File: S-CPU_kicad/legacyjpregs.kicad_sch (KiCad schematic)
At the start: 52 parts

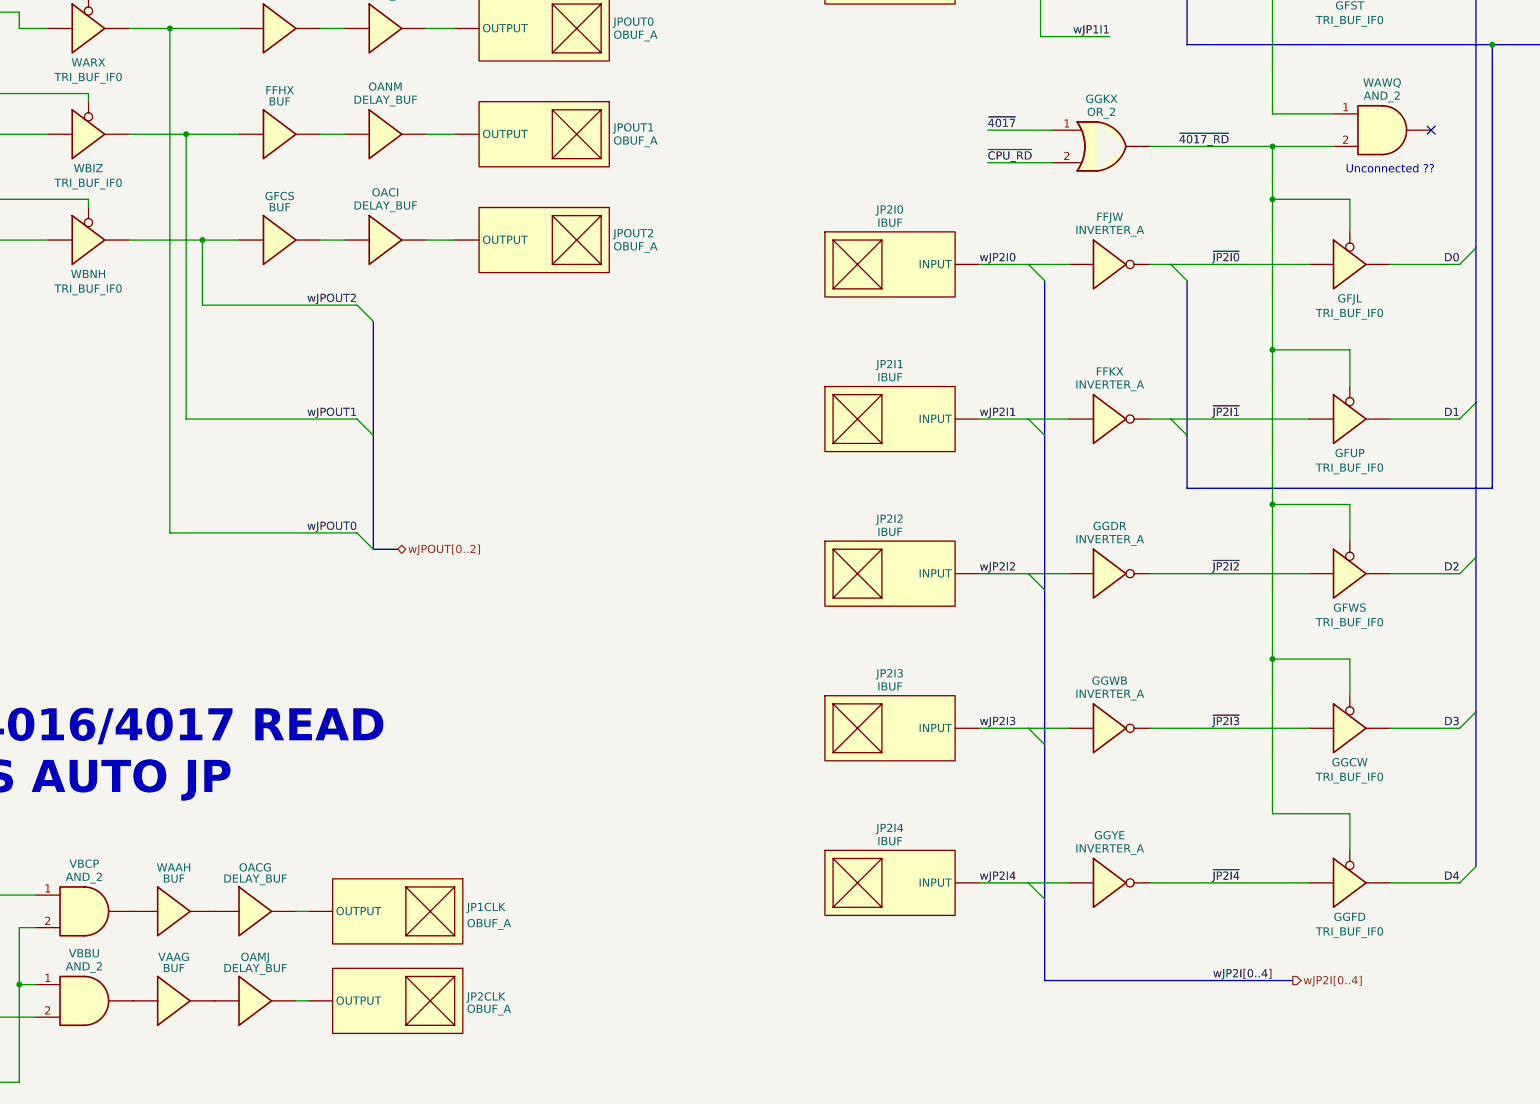
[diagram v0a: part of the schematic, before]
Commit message: Fixed VAWR which should have been an SR DFF (to fix issue #3 raised in github)
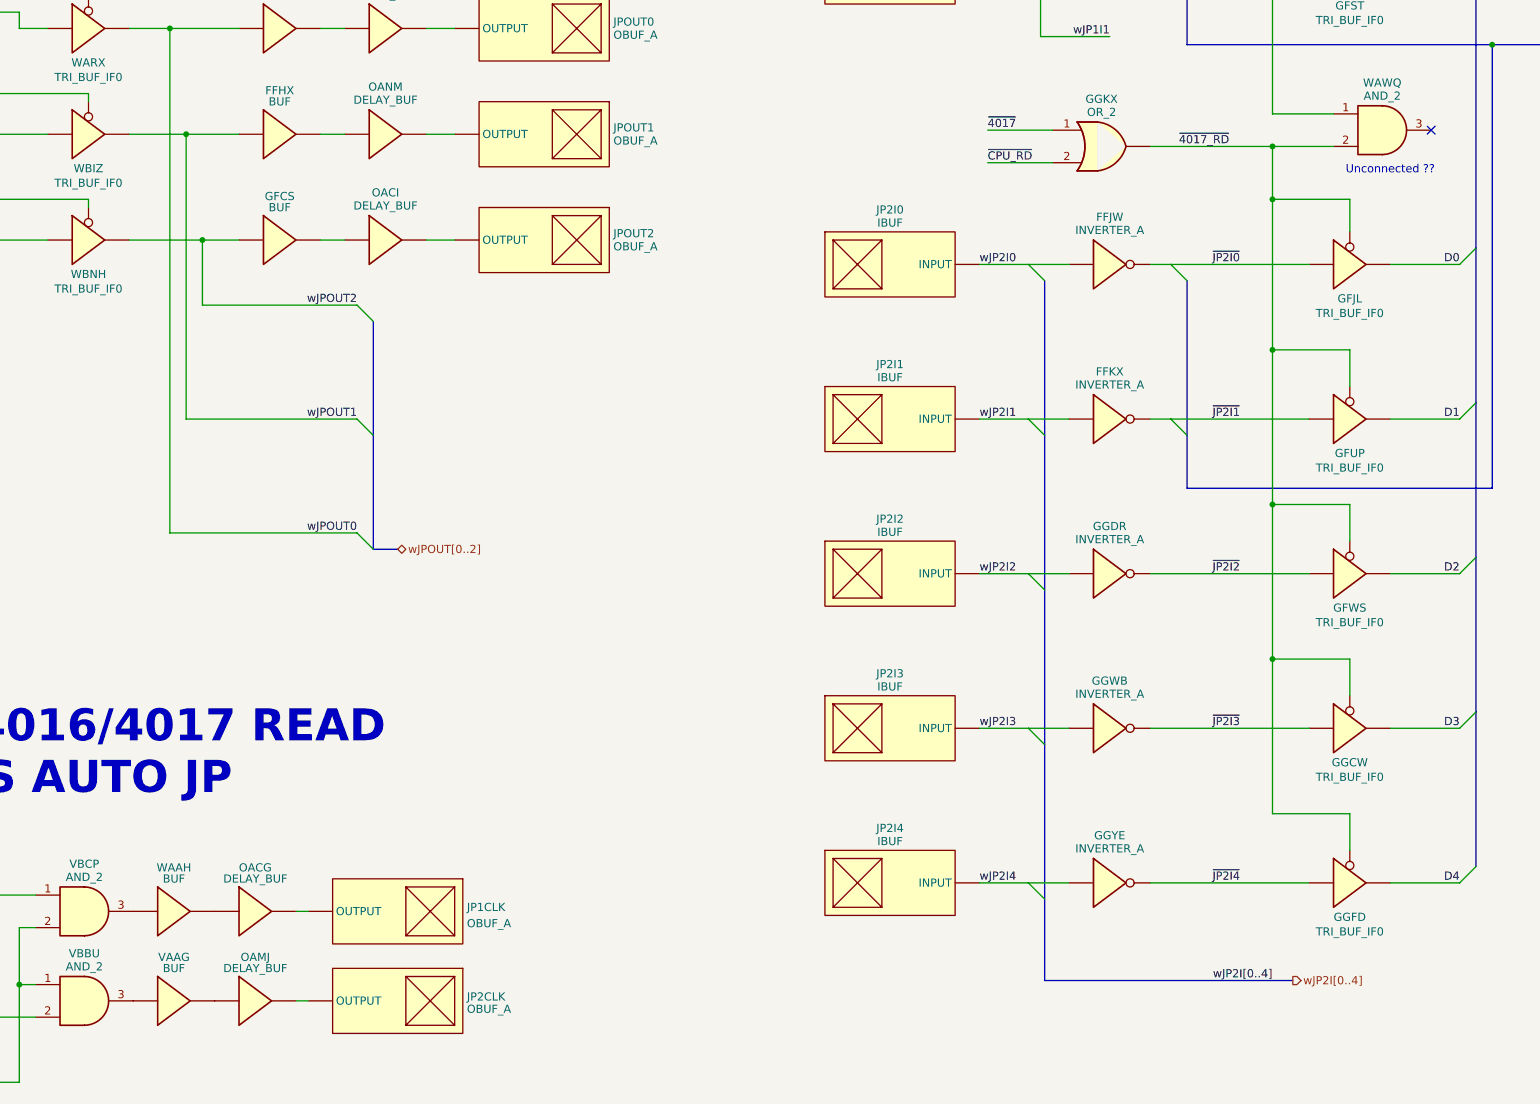
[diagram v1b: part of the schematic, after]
